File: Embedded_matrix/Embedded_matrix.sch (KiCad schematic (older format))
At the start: 16 parts

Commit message: RIP matrix for now lets use leds
updated
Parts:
- removed U?: TC20-11GWA, symbol led_matrix7x5:TC20-11GWA
- added D1, D10, D11, D12, D13, D14, D15, D16, D17, D18, D19, D2, D20, D21, D22, D23, D24, D25, D26, D27, D28, D29, D3, D30, D31, D32, D33, D34, D35, D36, D37, D38, D39, D4, D40, D41, D42, D43, D44, D45, D46, D47, D48, D49, D5, D50, D51, D52, D53, D54, D55, D56, D57, D58, D59, D6, D60, D61, D62, D63, D64, D7, D8, D9: LED, symbol Device:LED
- added R10: 560, symbol Device:R
- U1, U2: renamed from U?; footprint (none) -> Package_DIP:DIP-16_W7.62mm_Socket
- gave numbers to parts that had none: 13
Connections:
- net C1: now also D1.1 (K), D2.1 (K), D3.1 (K), D4.1 (K), D5.1 (K), D6.1 (K), D7.1 (K), D8.1 (K)
- net C2: now also D10.1 (K), D11.1 (K), D12.1 (K), D13.1 (K), D14.1 (K), D15.1 (K), D16.1 (K), D9.1 (K)
- net C3: now also D17.1 (K), D18.1 (K), D19.1 (K), D20.1 (K), D21.1 (K), D22.1 (K), D23.1 (K), D24.1 (K)
- net C4: now also D25.1 (K), D26.1 (K), D27.1 (K), D28.1 (K), D29.1 (K), D30.1 (K), D31.1 (K), D32.1 (K)
- net C5: now also D33.1 (K), D34.1 (K), D35.1 (K), D36.1 (K), D37.1 (K), D38.1 (K), D39.1 (K), D40.1 (K)
- net R1: now also D1.2 (A), D17.2 (A), D25.2 (A), D33.2 (A), D41.2 (A), D49.2 (A), D57.2 (A), D9.2 (A)
- net R2: now also D10.2 (A), D18.2 (A), D2.2 (A), D26.2 (A), D34.2 (A), D42.2 (A), D50.2 (A), D58.2 (A)
- net R3: now also D11.2 (A), D19.2 (A), D27.2 (A), D3.2 (A), D35.2 (A), D43.2 (A), D51.2 (A), D59.2 (A)
- net R4: now also D12.2 (A), D20.2 (A), D28.2 (A), D36.2 (A), D4.2 (A), D44.2 (A), D52.2 (A), D60.2 (A)
- net R5: now also D13.2 (A), D21.2 (A), D29.2 (A), D37.2 (A), D45.2 (A), D5.2 (A), D53.2 (A), D61.2 (A)
- net R6: now also D14.2 (A), D22.2 (A), D30.2 (A), D38.2 (A), D46.2 (A), D54.2 (A), D6.2 (A), D62.2 (A)
- net R7: now also D15.2 (A), D23.2 (A), D31.2 (A), D39.2 (A), D47.2 (A), D55.2 (A), D63.2 (A), D7.2 (A)
- net C6: now reaches U2.5 (QF)
- net C6: now also D41.1 (K), D42.1 (K), D43.1 (K), D44.1 (K), D45.1 (K), D46.1 (K), D47.1 (K), D48.1 (K)
- net C7: now reaches U2.6 (QG)
- net C7: now also D49.1 (K), D50.1 (K), D51.1 (K), D52.1 (K), D53.1 (K), D54.1 (K), D55.1 (K), D56.1 (K)
- net C8: now reaches U2.7 (QH)
- net C8: now also D57.1 (K), D58.1 (K), D59.1 (K), D60.1 (K), D61.1 (K), D62.1 (K), D63.1 (K), D64.1 (K)
- net at U1.7 (QH): now also R10.2
- new net R8: D16.2 (A), D24.2 (A), D32.2 (A), D40.2 (A), D48.2 (A), D56.2 (A), D64.2 (A), D8.2 (A), R10.1
- no-connect marks 6 -> 2

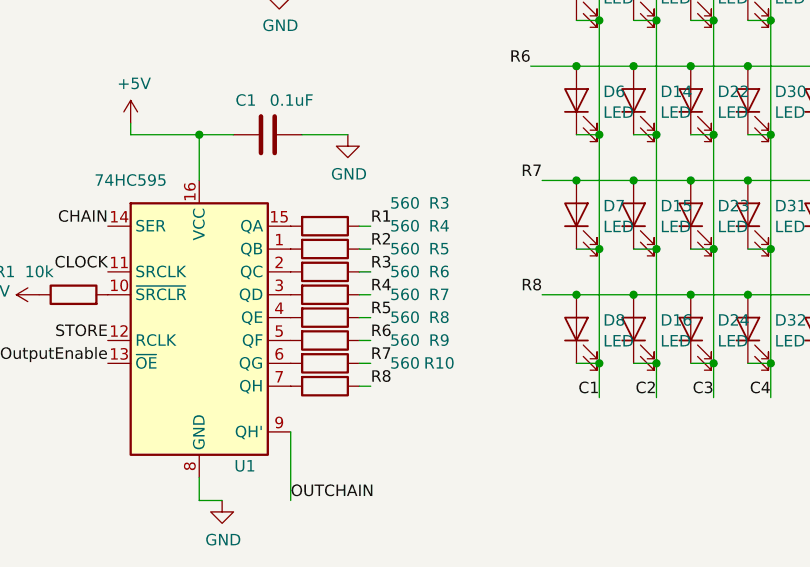
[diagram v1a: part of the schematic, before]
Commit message: Assigned PCB footprints
Might be checked again to see they are in left in stock on sites 

led -> https://www.elfa.se/sv/led-groen-mm-rnd-components-rnd-135-00038/p/30100035?q=led&filter_advisor_answerPath=_0_1&filter_advisor_campaignId=559&page=16&origPos=16&origPageSize=50&simi=99.85

-> capaictor -> https://www.elfa.se/en/ceramic-disk-capacitor-100-nf-50-vdc-mm-hitano-sf1h104z-l515b/p/16565659?q=*&filter_Category4=Ceramic+Disk+Capacitors&filter_Category3=Ceramic+Capacitors&filter_Buyable=1&filter_Capacitance~~uF=0.1&page=1&origPos=73&origPageSize=25&simi=98.9

pin female --> https://www.elfa.se/en/pin-header-female-rnd-connect-rnd-205-00647/p/30093667?queryFromSuggest=true

pin male --> https://www.elfa.se/en/pin-header-male-single-row-straight-without-shroud-wuerth-elektronik-61300611121/p/30024526

resitor SMD 0805, 10k,
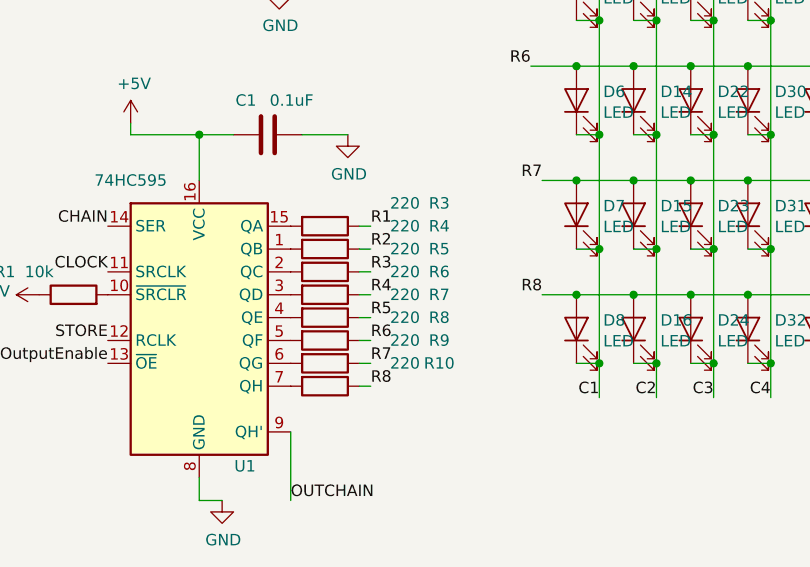
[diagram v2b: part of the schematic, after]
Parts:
- C1, C2: footprint (none) -> Capacitor_SMD:C_0805_2012Metric
- D1, D10, D11, D12, D13, D14, D15, D16, D17, D18, D19, D2, D20, D21, D22, D23, D24, D25, D26, D27, D28, D29, D3, D30, D31, D32, D33, D34, D35, D36, D37, D38, D39, D4, D40, D41, D42, D43, D44, D45, D46, D47, D48, D49, D5, D50, D51, D52, D53, D54, D55, D56, D57, D58, D59, D6, D60, D61, D62, D63, D64, D7, D8, D9: footprint (none) -> LED_THT:LED_D5.0mm
- J1, J2: footprint (none) -> Connector_PinHeader_2.54mm:PinHeader_1x07_P2.54mm_Vertical
- R1, R2: footprint (none) -> Resistor_SMD:R_0805_2012Metric_Pad1.15x1.40mm_HandSolder
- R10, R3, R4, R5, R6, R7, R8, R9: value 560 -> 220; footprint (none) -> Resistor_SMD:R_0805_2012Metric_Pad1.15x1.40mm_HandSolder
